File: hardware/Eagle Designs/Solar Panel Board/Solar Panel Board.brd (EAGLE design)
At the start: 82.4 x 96.7 mm, 34 parts, among them J1 MOLEX_503763-0291MOLEX_503763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, J2 MOLEX_503763-0491MOLEX_503763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

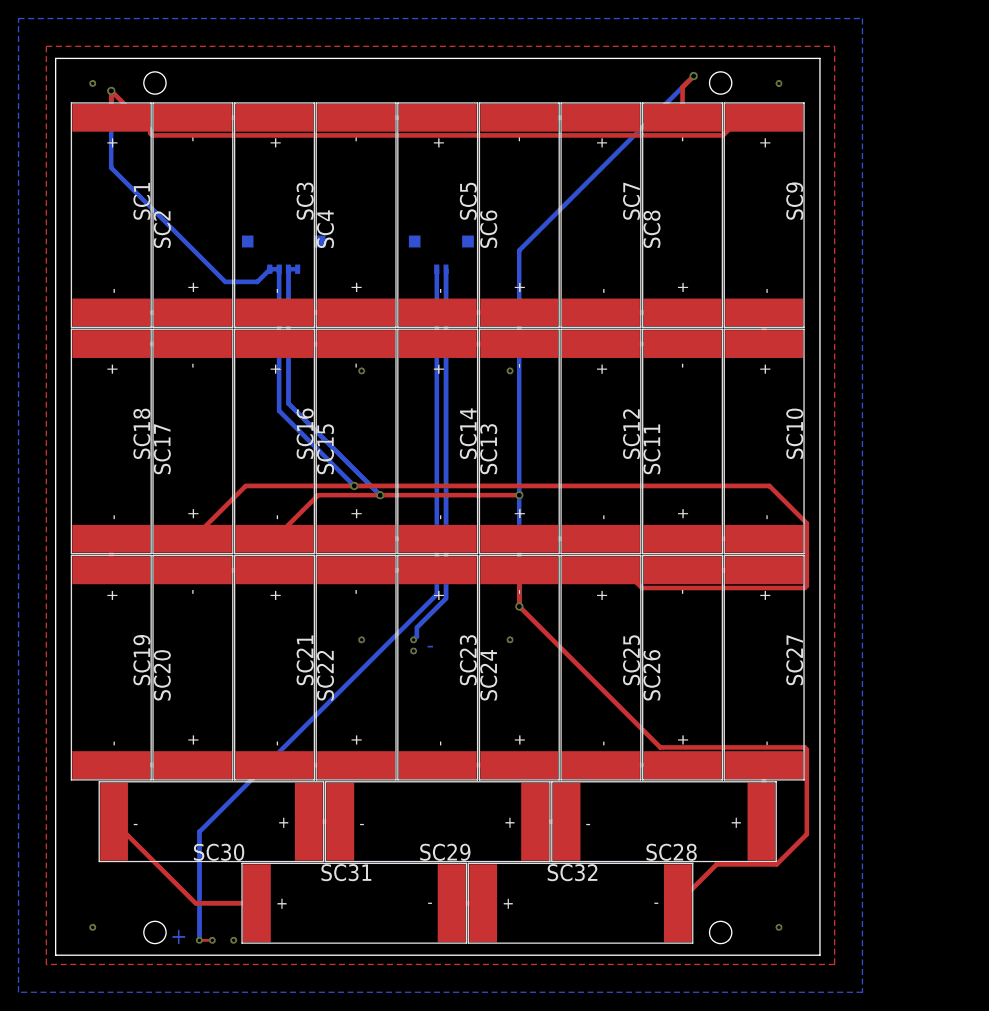
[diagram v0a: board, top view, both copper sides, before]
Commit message: Moved solar panel boards to Eagle folder, deleted redudant OBC files
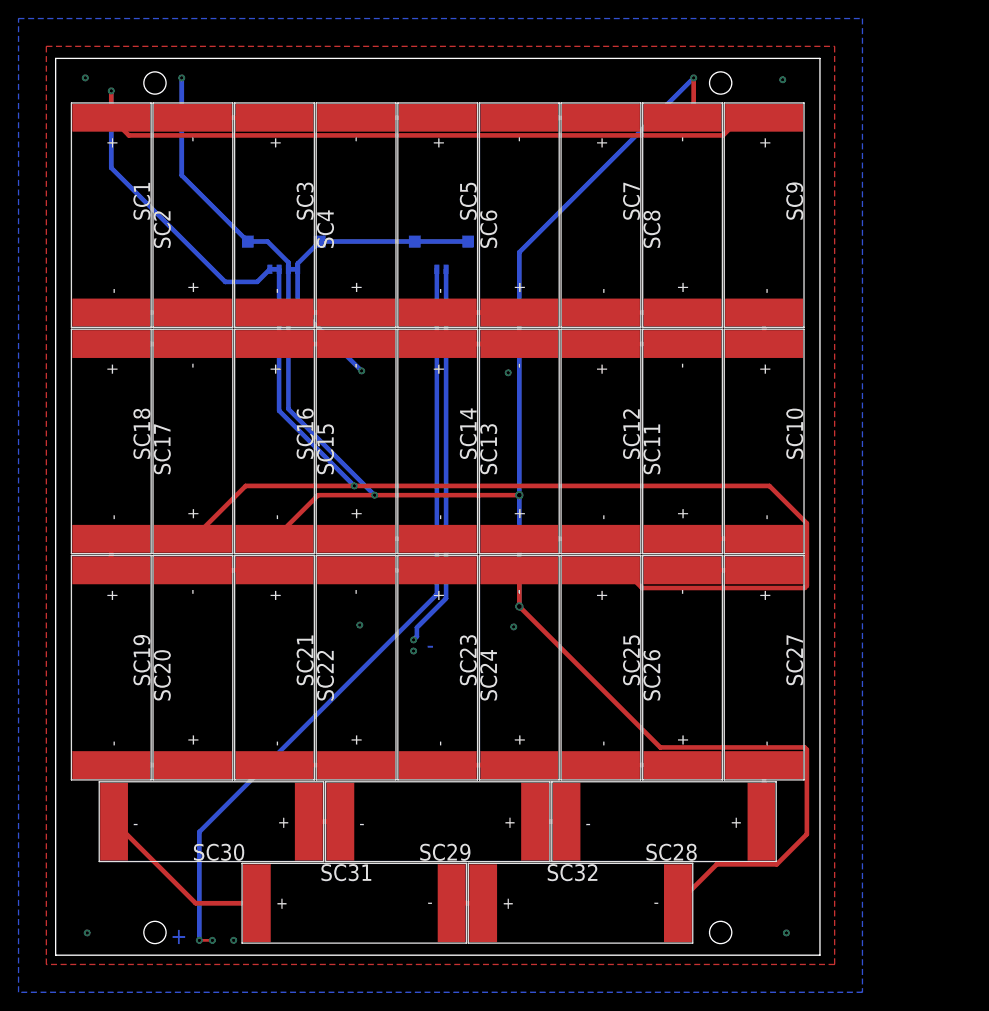
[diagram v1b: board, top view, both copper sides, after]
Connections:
- net GND: now also J1.3, J1.4, J2.5, J2.6
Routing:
- net GND: track 195.2 -> 255.0 mm, vias 12 -> 13
- net VCC: track 235.1 -> 233.7 mm
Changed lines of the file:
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@@
 <setting verticaltext="up"/>
 </settings>
-<grid distance="1" unitdist="mm" unit="mm" style="lines" multiple="1" display="yes" altdistance="0.1" altunitdist="mm" altunit="mm"/>
+<grid distance="0.2" unitdist="mm" unit="mm" style="lines" multiple="1" display="yes" altdistance="0.1" altunitdist="mm" altunit="mm"/>
 <layers>
 <layer number="1" name="Top" color="4" fill="1" visible="yes" active="yes"/>
@@
 <signal name="GND">
 <contactref element="J2" pad="4"/>
-<contactref element="SC8" pad="-"/>
-<contactref element="SC16" pad="-"/>
-<contactref element="SC24" pad="-"/>
-<contactref element="SC32" pad="-"/>
-<contactref element="J2" pad="3"/>
-<wire x1="25.1" y1="73.965" x2="25.1" y2="59.5" width="0.5" layer="16"/>
-<wire x1="25.1" y1="59.5" x2="35" y2="49.6" width="0.5" layer="16"/>
-<wire x1="25.1" y1="73.965" x2="26.1" y2="73.965" width="0.5" layer="16"/>
-<wire x1="23.6" y1="44.9" x2="28.3" y2="49.6" width="0.5" layer="1"/>
-<wire x1="28.3" y1="49.6" x2="35" y2="49.6" width="0.5" layer="1"/>
-<via x="35" y="49.6" extent="1-16" drill="0.5"/>
-<wire x1="35" y1="49.6" x2="50" y2="49.6" width="0.5" layer="1"/>
-<via x="50" y="49.6" extent="1-16" drill="0.5"/>
-<wire x1="50" y1="37.6" x2="50" y2="49.6" width="0.5" layer="16"/>
-<wire x1="50" y1="41.5" x2="50" y2="37.6" width="0.5" layer="1"/>
-<via x="50" y="37.6" extent="1-16" drill="0.5"/>
-<wire x1="81.0024" y1="22.16668125" x2="80.76668125" y2="22.4024" width="0.5" layer="1"/>
-<wire x1="65.1976" y1="22.4024" x2="50" y2="37.6" width="0.5" layer="1"/>
-<wire x1="80.76668125" y1="22.4024" x2="65.1976" y2="22.4024" width="0.5" layer="1"/>
-<wire x1="77.76668125" y1="9.7976" x2="81.0024" y2="13.03331875" width="0.5" layer="1"/>
-<wire x1="81.0024" y1="13.03331875" x2="81.0024" y2="22.16668125" width="0.5" layer="1"/>
-<wire x1="67.1" y1="5.6" x2="71.2976" y2="9.7976" width="0.5" layer="1"/>
-<wire x1="71.2976" y1="9.7976" x2="77.76668125" y2="9.7976" width="0.5" layer="1"/>
-<wire x1="67.6" y1="90.3" x2="67.6" y2="93.6" width="0.5" layer="1"/>
-<wire x1="67.6" y1="93.6" x2="68.8" y2="94.8" width="0.5" layer="1"/>
-<wire x1="50" y1="49.6" x2="50" y2="76" width="0.5" layer="16"/>
-<wire x1="50" y1="76" x2="68.8" y2="94.8" width="0.5" layer="16"/>
-<via x="68.8" y="94.8" extent="1-16" drill="0.5"/>
-<via x="33" y="34" extent="1-16" drill="0.35"/>
-<via x="49" y="34" extent="1-16" drill="0.35"/>
 <via x="33" y="63" extent="1-16" drill="0.35"/>
-<via x="49" y="63" extent="1-16" drill="0.35"/>
-<via x="4" y="94" extent="1-16" drill="0.35"/>
-<via x="78" y="94" extent="1-16" drill="0.35"/>
-<via x="78" y="3" extent="1-16" drill="0.35"/>
-<via x="4" y="3" extent="1-16" drill="0.35"/>
+<via x="13.6" y="94.6" extent="1-16" drill="0.35"/>
 <polygon width="0.1524" layer="1">
 <vertex x="-1" y="98"/>
@@
 <vertex x="-4" y="-4"/>
 </polygon>
+<contactref element="J1" pad="3"/>
+<contactref element="J1" pad="4"/>
+<contactref element="SC8" pad="-"/>
+<contactref element="SC16" pad="-"/>
+<contactref element="SC24" pad="-"/>
+<contactref element="SC32" pad="-"/>
+<wire x1="23.6" y1="44.9" x2="28.3" y2="49.6" width="0.5" layer="1"/>
+<via x="50" y="49.6" extent="1-16" drill="0.5"/>
+<wire x1="50" y1="37.6" x2="50" y2="49.6" width="0.5" layer="16"/>
+<wire x1="50" y1="41.5" x2="50" y2="37.6" width="0.5" layer="1"/>
+<via x="50" y="37.6" extent="1-16" drill="0.5"/>
+<wire x1="81.0024" y1="22.16668125" x2="80.76668125" y2="22.4024" width="0.5" layer="1"/>
+<wire x1="65.1976" y1="22.4024" x2="50" y2="37.6" width="0.5" layer="1"/>
+<wire x1="80.76668125" y1="22.4024" x2="65.1976" y2="22.4024" width="0.5" layer="1"/>
+<wire x1="77.76668125" y1="9.7976" x2="81.0024" y2="13.03331875" width="0.5" layer="1"/>
+<wire x1="81.0024" y1="13.03331875" x2="81.0024" y2="22.16668125" width="0.5" layer="1"/>
+<wire x1="67.1" y1="5.6" x2="71.2976" y2="9.7976" width="0.5" layer="1"/>
+<wire x1="71.2976" y1="9.7976" x2="77.76668125" y2="9.7976" width="0.5" layer="1"/>
+<wire x1="50" y1="49.6" x2="50" y2="75.8" width="0.5" layer="16"/>
+<wire x1="50" y1="75.8" x2="68.8" y2="94.6" width="0.5" layer="16"/>
+<contactref element="J2" pad="6"/>
+<contactref element="J2" pad="5"/>
+<contactref element="J2" pad="3"/>
+<wire x1="26.1" y1="73.965" x2="26.1" y2="69.9" width="0.5" layer="16"/>
+<wire x1="26.1" y1="69.9" x2="33" y2="63" width="0.5" layer="16"/>
+<wire x1="44.475" y1="76.955" x2="38.725" y2="76.955" width="0.5" layer="16"/>
+<wire x1="38.725" y1="76.955" x2="28.475" y2="76.955" width="0.5" layer="16"/>
+<wire x1="28.475" y1="76.955" x2="26.1" y2="74.58" width="0.5" layer="16"/>
+<wire x1="26.1" y1="74.58" x2="26.1" y2="73.965" width="0.5" layer="16"/>
+<wire x1="25.1" y1="73.965" x2="25.1" y2="74.7" width="0.5" layer="16"/>
+<wire x1="22.845" y1="76.955" x2="20.725" y2="76.955" width="0.5" layer="16"/>
+<wire x1="25.1" y1="74.7" x2="22.845" y2="76.955" width="0.5" layer="16"/>
+<wire x1="20.725" y1="76.955" x2="13.6" y2="84.08" width="0.5" layer="16"/>
+<wire x1="13.6" y1="84.08" x2="13.6" y2="94.6" width="0.5" layer="16"/>
+<via x="68.8" y="94.6" extent="1-16" drill="0.35"/>
+<wire x1="28.3" y1="49.6" x2="34.4" y2="49.6" width="0.5" layer="1"/>
+<wire x1="34.4" y1="49.6" x2="50" y2="49.6" width="0.5" layer="1"/>
+<via x="34.4" y="49.6" extent="1-16" drill="0.35"/>
+<wire x1="25.1" y1="58.9" x2="34.4" y2="49.6" width="0.5" layer="16"/>
+<wire x1="25.1" y1="73.965" x2="25.1" y2="58.9" width="0.5" layer="16"/>
+<wire x1="25.1" y1="73.965" x2="26.1" y2="73.965" width="0.5" layer="16"/>
+<wire x1="67.6" y1="90.3" x2="68.8" y2="91.5" width="0.5" layer="1"/>
+<wire x1="68.8" y1="91.5" x2="68.8" y2="94.6" width="0.5" layer="1"/>
+<via x="3.2" y="94.6" extent="1-16" drill="0.35"/>
+<via x="78.4" y="94.4" extent="1-16" drill="0.35"/>
+<via x="78.8" y="2.4" extent="1-16" drill="0.35"/>
+<via x="3.4" y="2.4" extent="1-16" drill="0.35"/>
+<via x="32.8" y="35.6" extent="1-16" drill="0.35"/>
+<via x="49.4" y="35.4" extent="1-16" drill="0.35"/>
+<via x="48.8" y="62.8" extent="1-16" drill="0.35"/>
 </signal>
 <signal name="VCC">
 <contactref element="J2" pad="1"/>
+<wire x1="23.1" y1="73.965" x2="21.735" y2="72.6" width="0.5" layer="16"/>
+<wire x1="21.735" y1="72.6" x2="18.3" y2="72.6" width="0.5" layer="16"/>
+<wire x1="18.3" y1="72.6" x2="6" y2="84.9" width="0.5" layer="16"/>
+<wire x1="71.96668125" y1="88.3976" x2="73.86908125" y2="90.3" width="0.5" layer="1"/>
 <contactref element="SC1" pad="+"/>
 <contactref element="SC9" pad="+"/>
 <contactref element="SC17" pad="+"/>
 <contactref element="SC25" pad="+"/>
-<contactref element="J2" pad="2"/>
-<wire x1="23.1" y1="73.965" x2="21.735" y2="72.6" width="0.5" layer="16"/>
-<wire x1="21.735" y1="72.6" x2="18.3" y2="72.6" width="0.5" layer="16"/>
 <wire x1="80.76668125" y1="39.5976" x2="81.0024" y2="39.83331875" width="0.5" layer="1"/>
 <wire x1="63.23331875" y1="39.5976" x2="80.76668125" y2="39.5976" width="0.5" layer="1"/>
@@
 <wire x1="58.8" y1="41.5" x2="61.33091875" y2="41.5" width="0.5" layer="1"/>
 <wire x1="61.33091875" y1="41.5" x2="63.23331875" y2="39.5976" width="0.5" layer="1"/>
-<wire x1="76.96908125" y1="50.6" x2="81.0024" y2="46.56668125" width="0.5" layer="1"/>
+<wire x1="81.0024" y1="46.56668125" x2="76.96908125" y2="50.6" width="0.5" layer="1"/>
 <wire x1="14.8" y1="44.9" x2="20.5" y2="50.6" width="0.5" layer="1"/>
+<contactref element="J2" pad="2"/>
+<wire x1="24.1" y1="58.7" x2="24.1" y2="73.965" width="0.5" layer="16"/>
+<wire x1="32.2" y1="50.6" x2="24.1" y2="58.7" width="0.5" layer="16"/>
+<via x="6" y="93.2" extent="1-16" drill="0.35"/>
+<via x="32.2" y="50.6" extent="1-16" drill="0.35"/>
 <wire x1="20.5" y1="50.6" x2="32.2" y2="50.6" width="0.5" layer="1"/>
-<wire x1="32.2" y1="50.6" x2="76.96908125" y2="50.6" width="0.5" layer="1"/>
+<wire x1="76.96908125" y1="50.6" x2="32.2" y2="50.6" width="0.5" layer="1"/>
+<wire x1="6" y1="90.3" x2="6" y2="93.2" width="0.5" layer="1"/>
+<wire x1="7.9024" y1="88.3976" x2="6" y2="90.3" width="0.5" layer="1"/>
+<wire x1="71.96668125" y1="88.3976" x2="7.9024" y2="88.3976" width="0.5" layer="1"/>
+<wire x1="6" y1="84.9" x2="6" y2="93.2" width="0.5" layer="16"/>
+<wire x1="73.86908125" y1="90.3" x2="76.4" y2="90.3" width="0.5" layer="1"/>
 <wire x1="23.1" y1="73.965" x2="24.1" y2="73.965" width="0.5" layer="16"/>
-<wire x1="24.1" y1="73.965" x2="24.1" y2="58.7" width="0.5" layer="16"/>
-<wire x1="24.1" y1="58.7" x2="32.2" y2="50.6" width="0.5" layer="16"/>
-<via x="32.2" y="50.6" extent="1-16" drill="0.5"/>
-<wire x1="6" y1="93.2" x2="6" y2="90.3" width="0.5" layer="1"/>
-<wire x1="18.3" y1="72.6" x2="6" y2="84.9" width="0.5" layer="16"/>
-<wire x1="6" y1="84.9" x2="6" y2="93.2" width="0.5" layer="16"/>
-<via x="6" y="93.2" extent="1-16" drill="0.5"/>
-<wire x1="10.43331875" y1="88.3976" x2="10.1976" y2="88.63331875" width="0.5" layer="1"/>
-<wire x1="76.4" y1="90.3" x2="73.86908125" y2="90.3" width="0.5" layer="1"/>
-<wire x1="10.1976" y1="88.63331875" x2="10.1976" y2="89.0024" width="0.5" layer="1"/>
-<wire x1="73.86908125" y1="90.3" x2="71.96668125" y2="88.3976" width="0.5" layer="1"/>
-<wire x1="71.96668125" y1="88.3976" x2="10.43331875" y2="88.3976" width="0.5" layer="1"/>
-<wire x1="10.1976" y1="89.0024" x2="6" y2="93.2" width="0.5" layer="1"/>
 </signal>
 </signals>

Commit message: Updated solar panel boards
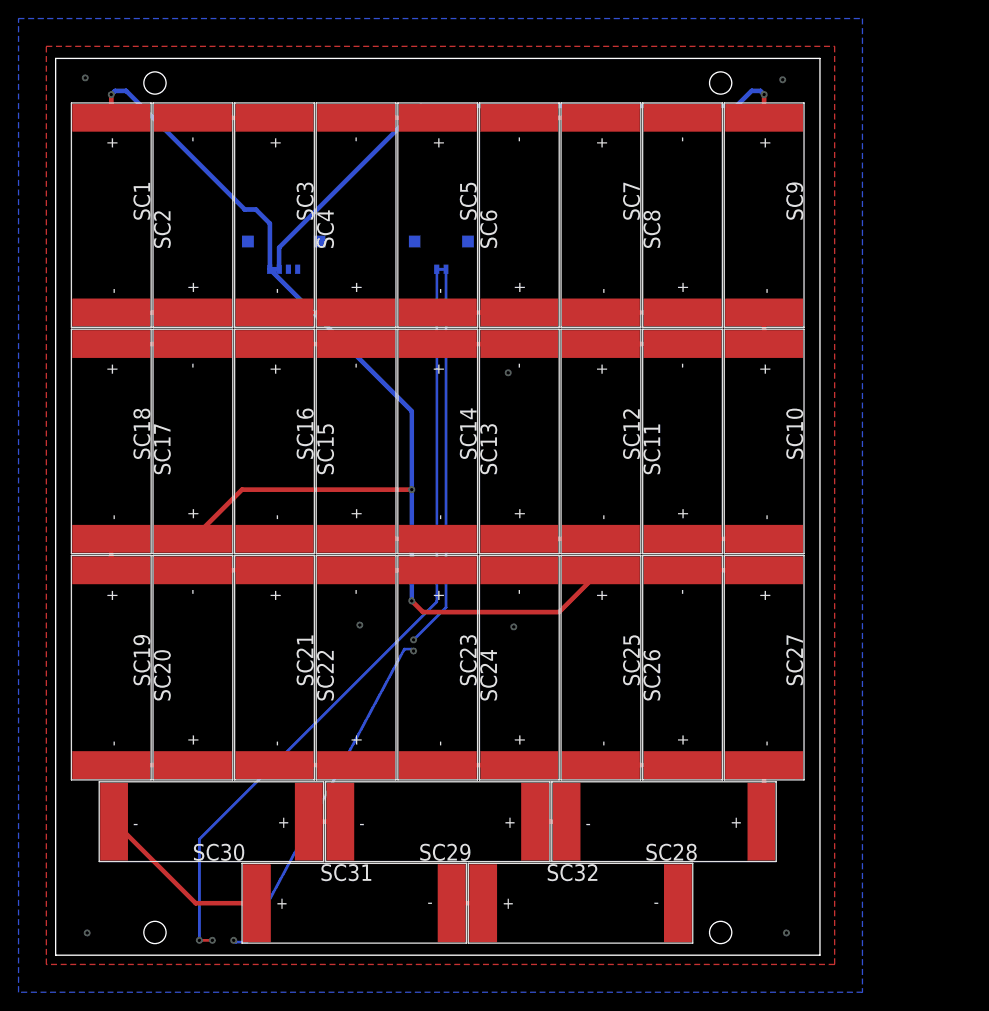
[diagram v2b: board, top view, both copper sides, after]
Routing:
- net GND: track 255.0 -> 0.00 mm, vias 13 -> 7
- net VCC: track 233.7 -> 186.6 mm, vias 2 -> 4
- net N$1: track 22221.6 -> 22222.6 mm

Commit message: Solar panel board changes
Added temp sensor and external connector to solar panel board; updated solar panel board BOM
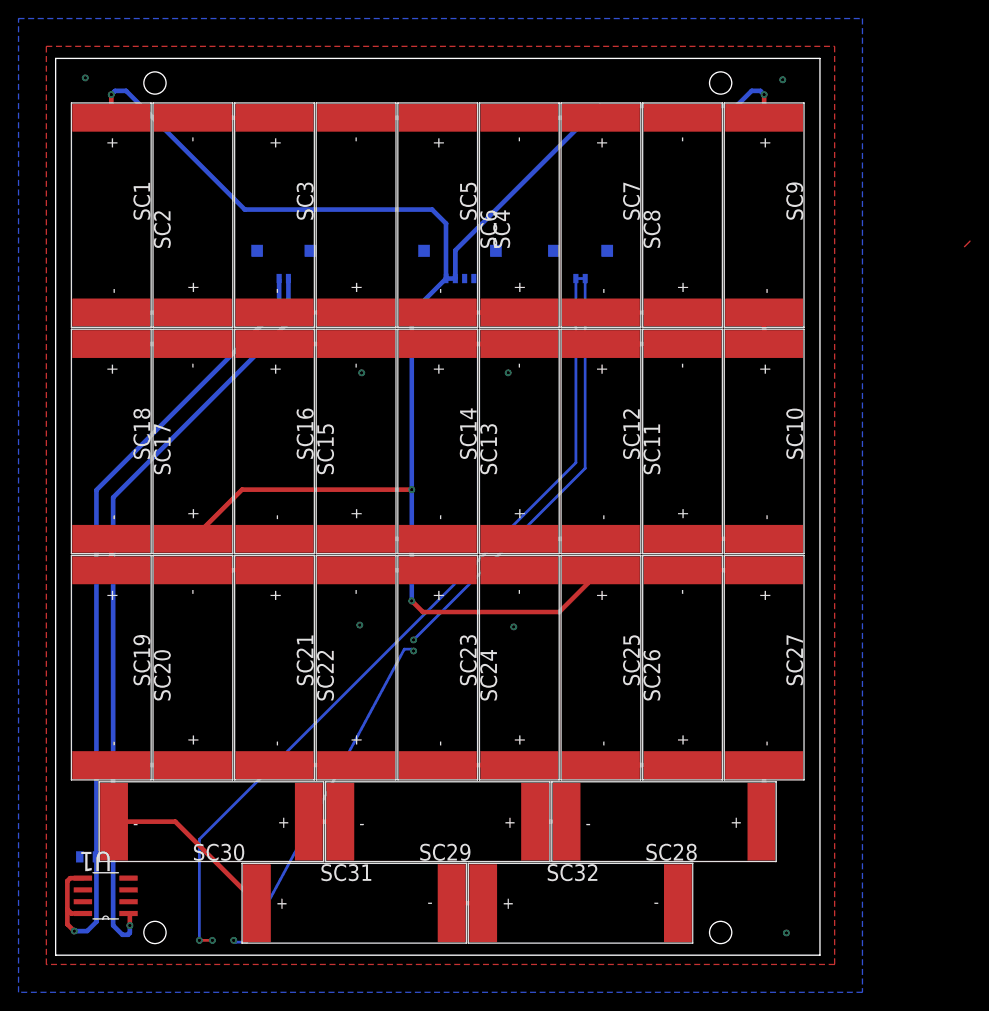
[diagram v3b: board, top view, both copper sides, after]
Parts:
- added C1: (no value), HSFL_Main_Library:0805
- added J3: MOLEX_503763-0291MOLEX_503763-0291_0_0, Molex - 503763-0291:MOLEX_503763-0291_0
- added U1: TMP36GSZ, TMP36GSZ:SOIC127P600X175-8N
- moved J2 19.0 mm to (43.6, 75.4)
- moved J1 15.0 mm to (56.6, 75.4)
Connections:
- new net VOUT: J3.2, U1.1
- new net VS+: C1.1, J3.1, U1.5, U1.8
- net GND: now also C1.2, J3.3, J3.4, U1.4
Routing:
- net VS+: track 0.00 -> 89.7 mm, vias 0 -> 1
- net VOUT: track 0.00 -> 82.0 mm, vias 0 -> 1
- net N$1: track 22222.6 -> 22233.0 mm
- net VCC: track 186.6 -> 182.6 mm
- net N$30: track 0.00 -> 0.85 mm

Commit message: Added values to resistors and capacitors
Payload - added 3.3k value to pullup resistors for H-bridges
Solar Panel Board - added 0.1uF value to capacitor for temp sensor
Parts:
- C1: value (none) -> 0.1uF
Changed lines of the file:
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@@
 <attribute name="TEMPERATURE_RANGE_LOW" value="-40°C" x="24.6" y="75.4" size="1.778" layer="28" rot="MR0" display="off"/>
 </element>
-<element name="C1" library="HSFL_Main_Library" package="0805" value="" x="3.5" y="10.6" smashed="yes" rot="MR0">
+<element name="C1" library="HSFL_Main_Library" package="0805" value="0.1uF" x="3.5" y="10.6" smashed="yes" rot="MR0">
 <attribute name="NAME" x="2.678" y="11.6795" size="0.8128" layer="26" font="vector" ratio="15" rot="SMR0"/>
 <attribute name="VALUE" x="5.278" y="8.5045" size="0.8128" layer="28" font="vector" ratio="15" rot="SMR0"/>
